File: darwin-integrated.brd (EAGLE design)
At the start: 96 x 62 mm, 41 parts

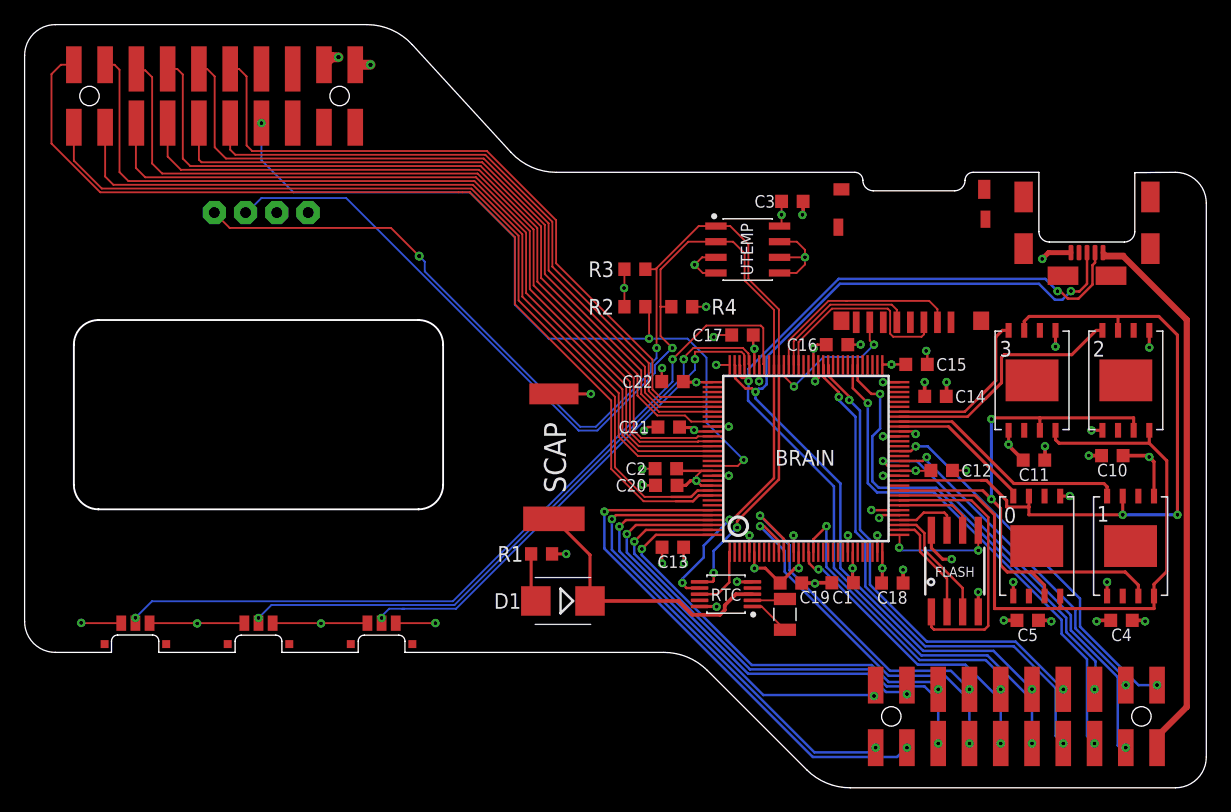
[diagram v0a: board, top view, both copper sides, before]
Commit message: Corrected VDDCORE and VSW errors.
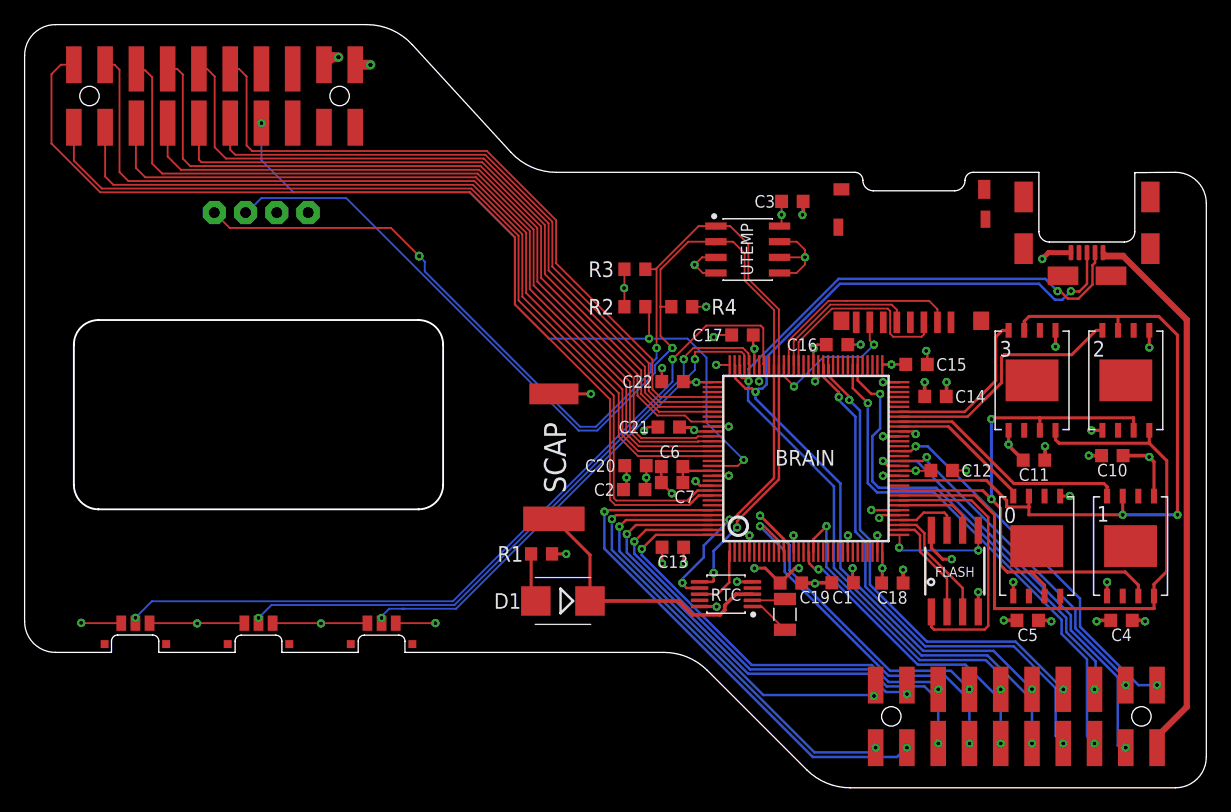
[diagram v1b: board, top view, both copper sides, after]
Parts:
- added C6: .1u, rcl:C0603K
- added C7: 4.7u, rcl:C0603K
- moved C2 3.08 mm to (52.5, 25.2)
- moved C20 2.97 mm to (52.6, 27.2)
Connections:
- new net N$6: BRAIN.115, C6.1, C7.1
- net 3V3: no longer BRAIN.115, BRAIN.117
- net GND: now also C6.2, C7.2
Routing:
- net 3V3: track 64.6 -> 56.7 mm, vias 29 -> 30
- net N$6: track 0.00 -> 3.85 mm
- net GND: track 91.4 -> 94.6 mm
- net SWDIO: track 80.1 -> 81.9 mm
- net SWCLK: track 72.6 -> 74.3 mm

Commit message: Added pullup resistor for QSPI Flash chip select.
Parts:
- added R5: (no value), rcl:R0603
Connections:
- net 3V3: now also R5.2
- net QSPI_CS: now also R5.1
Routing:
- net 3V3: track 56.7 -> 60.4 mm
- net QSPI_CS: track 22.7 -> 25.4 mm
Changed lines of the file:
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@@
 <setting verticaltext="up"/>
 </settings>
-<grid distance="1" unitdist="mil" unit="mil" style="lines" multiple="1" display="no" altdistance="0.1" altunitdist="mm" altunit="mm"/>
+<grid distance="1" unitdist="mm" unit="mm" style="lines" multiple="1" display="no" altdistance="0.1" altunitdist="mm" altunit="mm"/>
 <layers>
 <layer number="1" name="Top" color="4" fill="1" visible="yes" active="yes"/>
@@
 <attribute name="SPICEPREFIX" value="C" x="55.6" y="25.8" size="1.778" layer="27" rot="R180" display="off"/>
 </element>
+<element name="R5" library="rcl" library_urn="urn:adsk.eagle:library:334" package="R0603" package3d_urn="urn:adsk.eagle:package:23555/3" value="" x="73.4824" y="13.8908" smashed="yes" rot="R180">
+<attribute name="NAME" x="74.1174" y="13.2558" size="1.27" layer="25" rot="R180"/>
+<attribute name="SPICEPREFIX" value="R" x="73.4824" y="13.8908" size="1.778" layer="27" rot="R180" display="off"/>
+<attribute name="VALUE" x="74.1174" y="15.7958" size="1.27" layer="27" rot="R180"/>
+</element>
 </elements>
 <signals>
@@
 <wire x1="79.9092875" y1="24.3628" x2="81.2882" y2="22.9838875" width="0.2032" layer="1"/>
 <wire x1="81.2882" y1="14.1519125" x2="80.9924875" y2="13.8562" width="0.2032" layer="1"/>
-<wire x1="80.9924875" y1="13.8562" x2="76.8686" y2="13.8562" width="0.2032" layer="1"/>
+<wire x1="80.9924875" y1="13.8562" x2="77" y2="13.8562" width="0.2032" layer="1"/>
+<wire x1="77" y1="13.8562" x2="76.8686" y2="13.8562" width="0.2032" layer="1"/>
 <wire x1="81.2882" y1="22.9838875" x2="81.2882" y2="14.1519125" width="0.2032" layer="1"/>
 <wire x1="76.8686" y1="13.8562" x2="76.6654" y2="14.0594" width="0.2032" layer="1"/>
 <wire x1="76.6654" y1="14.0594" x2="76.6654" y2="15.291" width="0.2032" layer="1"/>
+<contactref element="R5" pad="1"/>
+<wire x1="74.3324" y1="13.8908" x2="74.367" y2="13.8562" width="0.1524" layer="1"/>
+<wire x1="77" y1="13.8562" x2="74.367" y2="13.8562" width="0.2" layer="1"/>
 </signal>
 <signal name="FLASH_MOSI">
@@
 <wire x1="53.5" y1="26.2" x2="53.502" y2="26.202" width="0.2032" layer="1"/>
 <wire x1="53.502" y1="27.1682" x2="53.502" y2="26.202" width="0.2032" layer="1"/>
+<contactref element="R5" pad="2"/>
+<wire x1="72.6324" y1="13.8908" x2="72.6324" y2="17.6196" width="0.2" layer="1"/>
+<wire x1="72.6324" y1="17.6196" x2="72.617" y2="17.635" width="0.2" layer="1"/>
 <wire x1="70.28" y1="18.85" x2="70.28" y2="20.15" width="0" layer="19" extent="1-1"/>
 <wire x1="65.88" y1="20.15" x2="65.88" y2="18.8504" width="0" layer="19" extent="1-1"/>

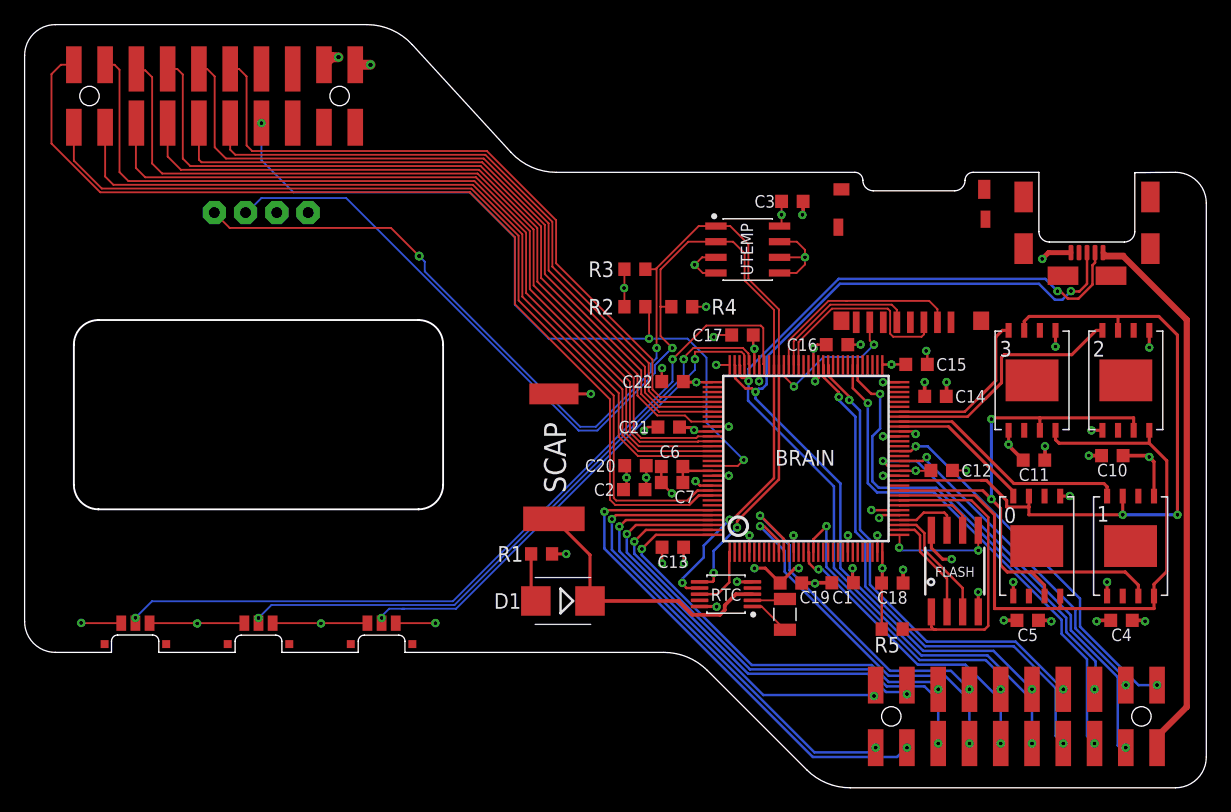
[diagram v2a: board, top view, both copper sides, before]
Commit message: Moved SD card, USB, and Temp sensor posistions for better cable access. Expanded screen window by 2MM.
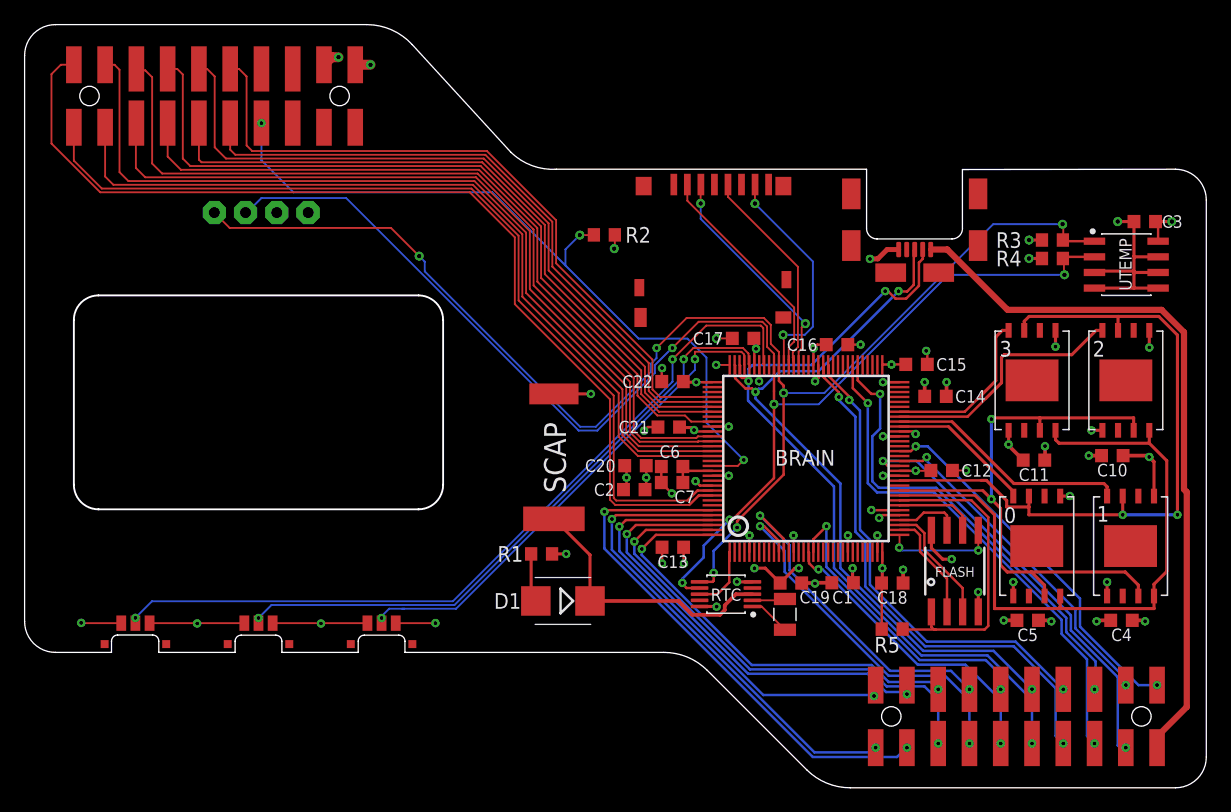
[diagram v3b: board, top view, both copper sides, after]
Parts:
- moved R3 34.0 mm to (86.5, 45.5)
- moved UTEMP 30.8 mm to (92.5, 43.5)
- moved R4 30.4 mm to (86.5, 44.0), turned to 180 degrees
- moved C3 28.7 mm to (94.0, 47.0), turned to 180 degrees
- moved U$8 14.0 mm to (75.3, 45.6)
- moved U$9 11.8 mm to (63.4, 49.1), turned to 180 degrees
- moved R2 6.34 mm to (50.1, 45.9), turned to 0 degrees
- moved C17 0.28 mm to (61.4, 37.5)
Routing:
- net CORE_SDA: track 95.8 -> 114.7 mm, vias 4 -> 6
- net CORE_SCL: track 94.7 -> 112.9 mm, vias 3 -> 5
- net D+: track 75.5 -> 59.4 mm
- net D-: track 79.7 -> 65.1 mm
- net V5: track 46.2 -> 58.2 mm
- net SD_MISO: track 12.0 -> 18.7 mm
- net GND: track 94.6 -> 100.7 mm, vias 44 -> 42
- net SD_SCK: track 12.7 -> 17.8 mm
- net SD_SS: track 16.7 -> 18.9 mm
- net SD_MOSI: track 16.3 -> 18.4 mm, vias 0 -> 2
- net RESET: track 64.0 -> 62.2 mm
- net 3V3: track 60.4 -> 60.7 mm, vias 30 -> 31
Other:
- outline, holes or cut-outs redrawn

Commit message: Fixed Memory footprints. CAM output for TA2. Reorganized CAM files.
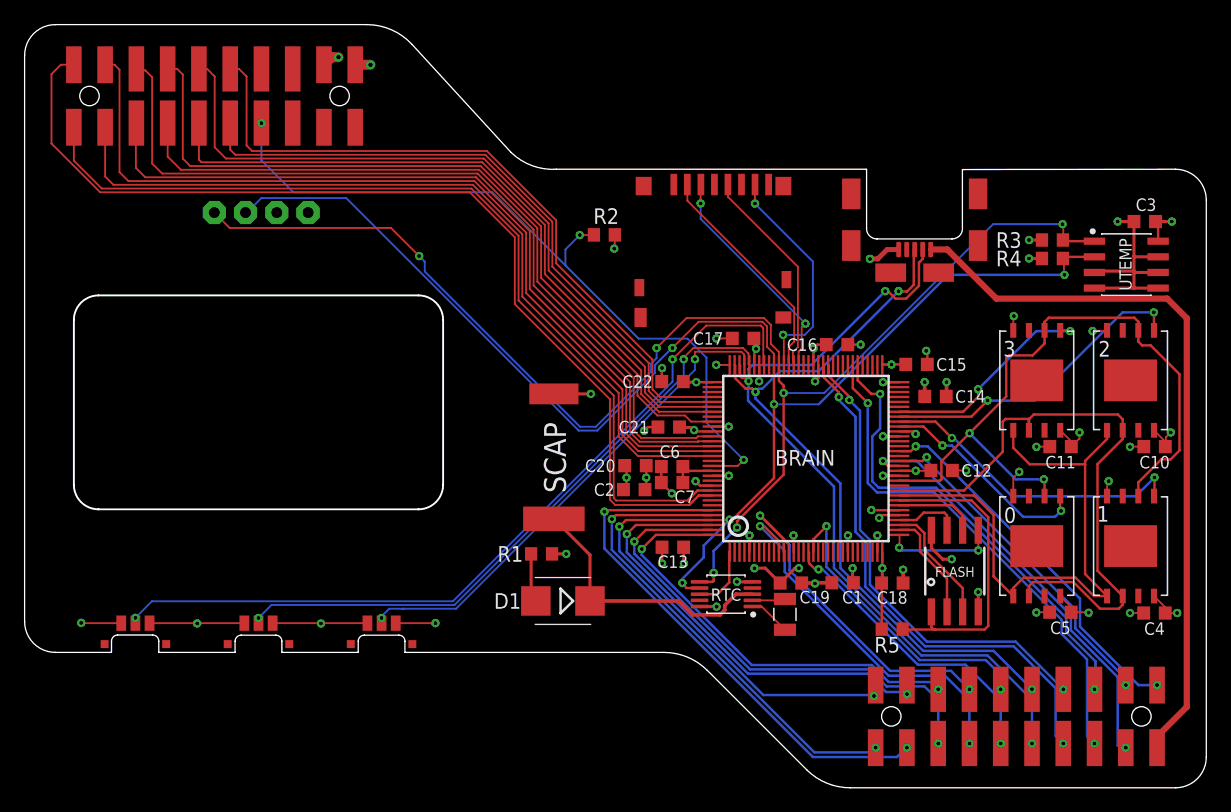
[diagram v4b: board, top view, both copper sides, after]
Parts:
- moved C10 3.51 mm to (94.8, 28.7), turned to 180 degrees
- moved C4 2.74 mm to (94.8, 15.2), turned to 180 degrees
- moved C5 2.74 mm to (87.1, 15.3), turned to 180 degrees
- moved C11 2.42 mm to (87.2, 28.7), turned to 180 degrees
- moved U$5 0.38 mm to (92.8, 34.1)
- moved U$6 0.38 mm to (85.2, 34.1)
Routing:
- net FLASH_MOSI: track 54.0 -> 47.5 mm
- net FLASH_S0: track 11.8 -> 17.6 mm, vias 0 -> 2
- net FLASH_S1: track 19.8 -> 25.4 mm, vias 0 -> 2
- net FLASH_S2: track 20.6 -> 25.6 mm, vias 0 -> 2
- net FLASH_S3: track 13.7 -> 17.8 mm, vias 0 -> 2
- net 3V3: track 60.7 -> 64.1 mm, vias 31 -> 28
- net GND: track 100.7 -> 98.6 mm, vias 42 -> 43
- net FLASH_SCK: track 48.7 -> 50.6 mm, vias 2 -> 0
- net FLASH_MISO: track 56.5 -> 55.5 mm
- net V5: track 58.2 -> 59.0 mm
